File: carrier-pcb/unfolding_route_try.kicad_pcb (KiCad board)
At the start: 2 copper layers, 57 x 74.6 mm, 71 parts, among them J1 USB_C_Receptacle_USB2.0, J2 Conn_01x01_Female, J3 1-338068-8, J4 Conn_01x01_Female, J5 Conn_01x01_Female, J6 Conn_01x01_Female, U1 TCA9548APWR, U10 DRV2605LDGS, U11 DRV2605LDGS, U12 BMX160, U13 TPD2EUSB30, U2 TCA9548APWR, U3 DRV2605LDGS, U4 DRV2605LDGS, U5 DRV2605LDGS, U6 DRV2605LDGS, U7 DRV2605LDGS, U8 DRV2605LDGS, U9 DRV2605LDGS

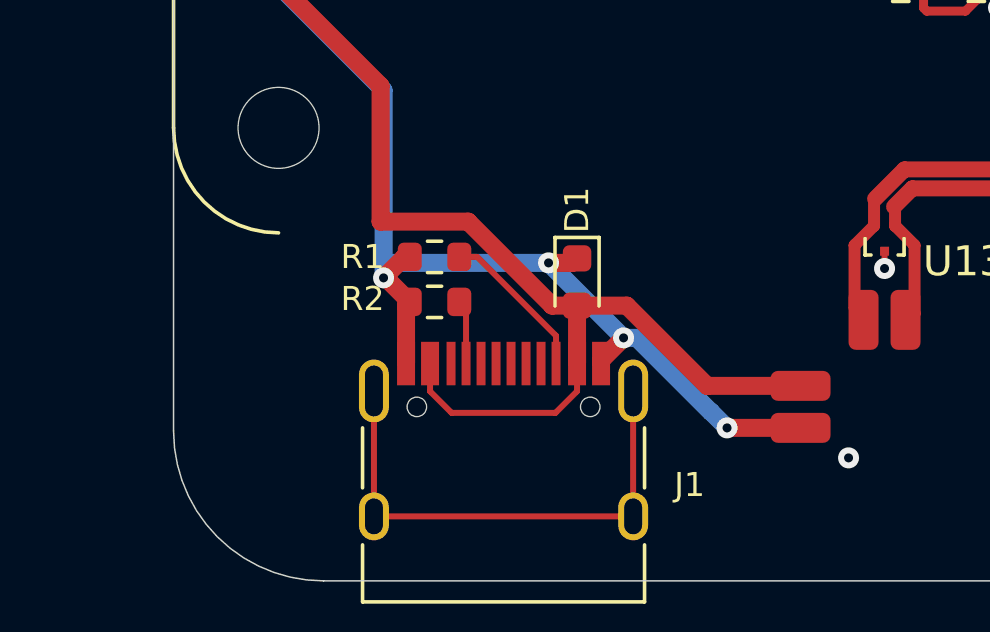
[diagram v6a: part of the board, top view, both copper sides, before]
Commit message: change diode footprint
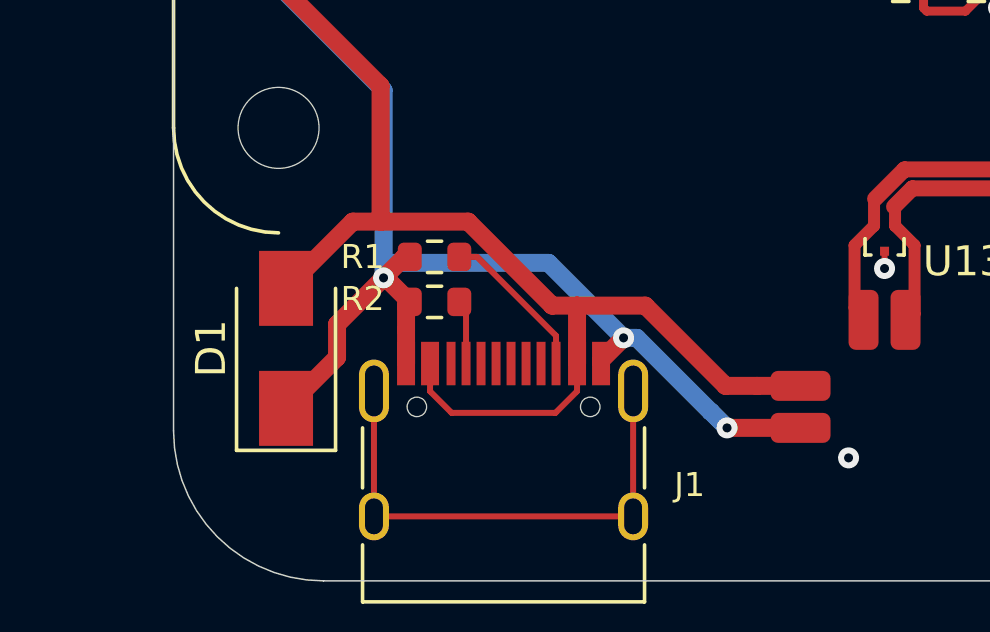
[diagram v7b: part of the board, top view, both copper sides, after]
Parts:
- D1: value RND SMBJ5A -> SMA6J5.0A; footprint Diode_SMD:D_0603_1608Metric -> Diode_SMD:D_SMA
- moved D1 9.95 mm to (118.8, 95.2), turned to 90 degrees
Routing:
- net GND: track 62.2 -> 66.9 mm, vias 80 -> 79
- net +5V: track 53.3 -> 57.3 mm

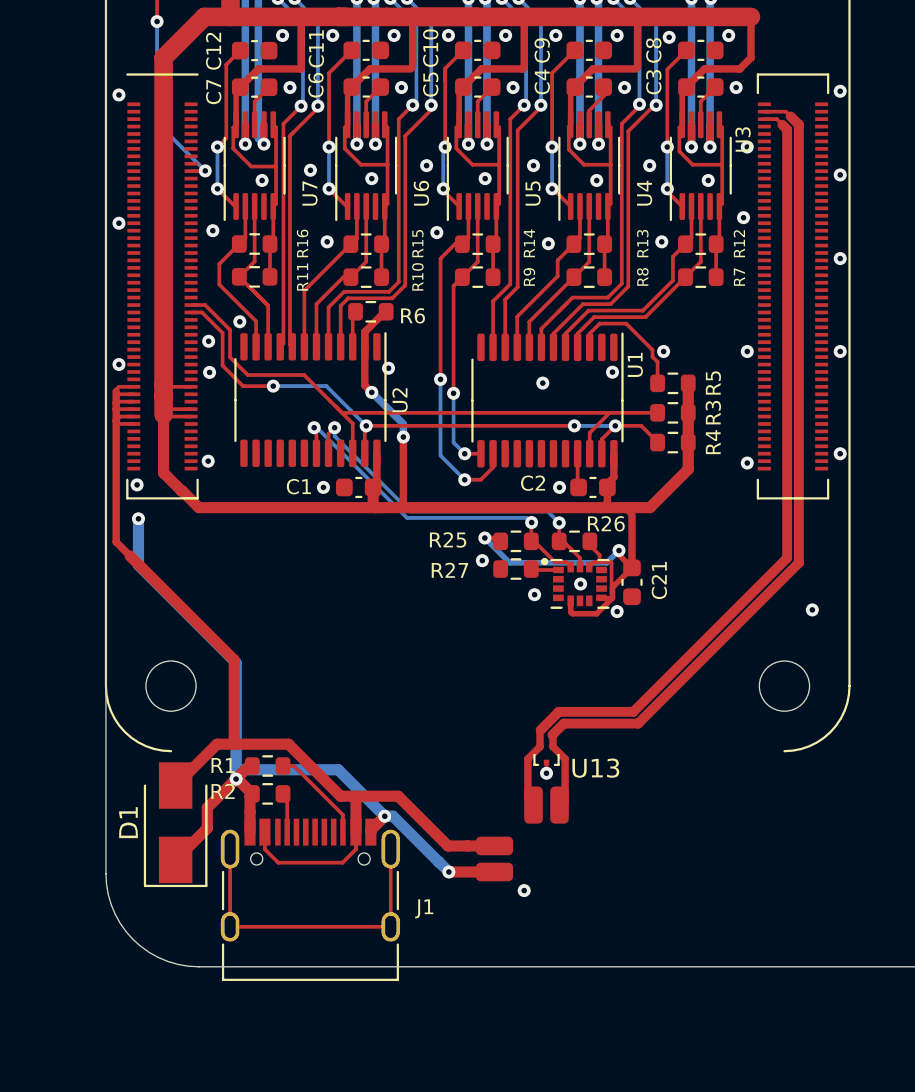
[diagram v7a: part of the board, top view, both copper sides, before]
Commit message: change ESD protection. change usb plug. reroute
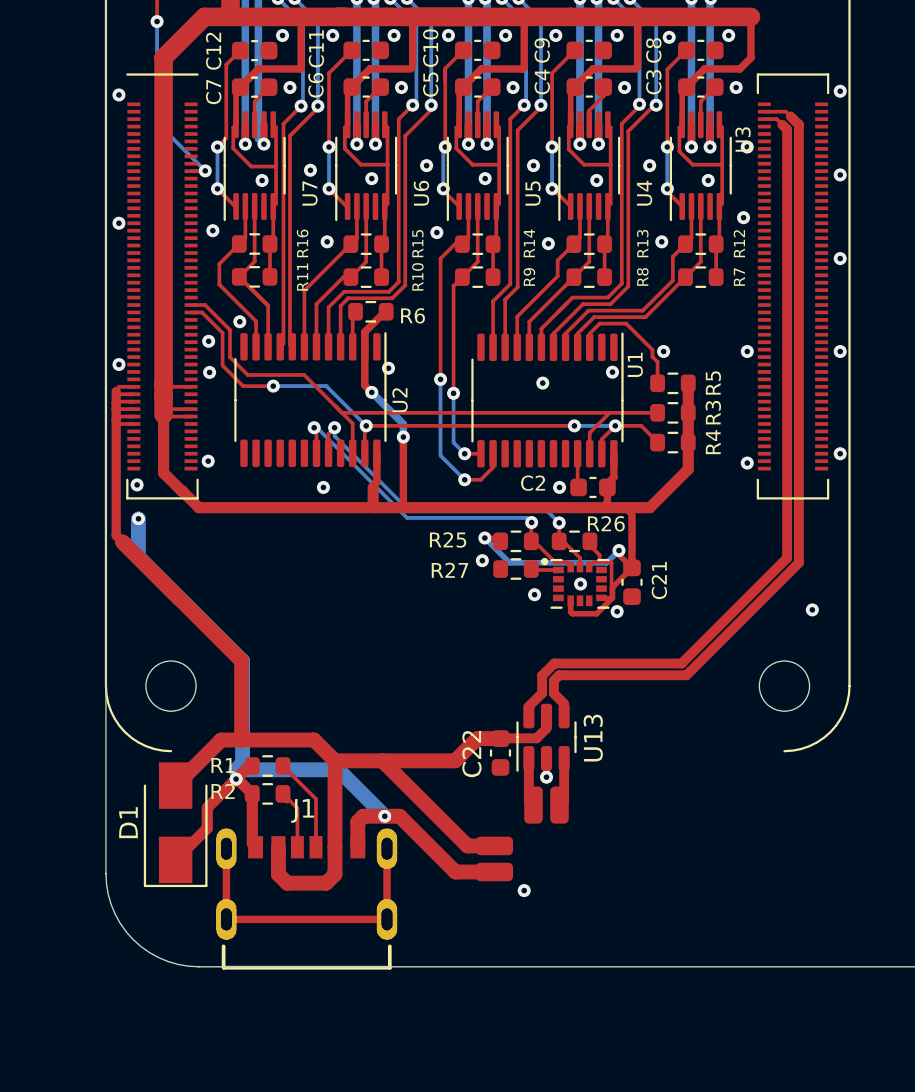
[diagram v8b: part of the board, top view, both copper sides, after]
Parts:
- removed C1: 1u, Capacitor_SMD:C_0603_1608Metric
- added C22: 100n, Capacitor_SMD:C_0603_1608Metric, F.Cu at (136.2, 91.5)
- J1: value USB_C_Receptacle_USB2.0 -> USB4125-GF-A_REVA; footprint Connector_USB:USB_C_Receptacle_HRO_TYPE-C-31-M-12 -> USB4125-GF-A_REVA:GCT_USB4125-GF-A_REVA
- U13: value TPD2EUSB30 -> USBLC6-2SC6; footprint Package_TO_SOT_SMD:Texas_DRT-3 -> Package_TO_SOT_SMD:SOT-23-6
- moved J1 3.16 mm to (125.8, 96.7)
- moved U13 0.94 mm to (138.7, 90.7), turned to 90 degrees
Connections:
- J1 pad S1: unconnected-(J1-PadS1) -> Net-(J1-PadS1)
- Module1 pad 103: USB_D- -> USB_D-out
- Module1 pad 105: USB_D+ -> USB_D+out
- U13 pad 1: USB_D- -> USB_D+
- U13 pad 2: USB_D+ -> GND
- U13 pad 3: GND -> USB_D-
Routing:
- net USB_D-: track 47.0 -> 2.90 mm
- net USB_D-out: track 0.00 -> 43.0 mm
- net USB_D+: track 46.1 -> 3.18 mm
- net USB_D+out: track 0.00 -> 42.8 mm
- net unconnected-(J1-PadS1): track 17.0 -> 0.00 mm
- net +5V: track 57.3 -> 73.7 mm
- net Net-(J1-PadS1): track 0.00 -> 16.2 mm
- net GND: track 66.9 -> 70.4 mm, vias 79 -> 78
- net Net-(J1-PadA5): track 1.95 -> 3.49 mm
